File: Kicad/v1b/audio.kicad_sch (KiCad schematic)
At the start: 39 parts, among them U16 74HC139, U17 74HC153, U18 74HC670, U19 74HC670, U20 82C54, U21 82C54 (PLCC), U22 74HC165, U23 74HC165, U24 74HC165, U25 74HC165

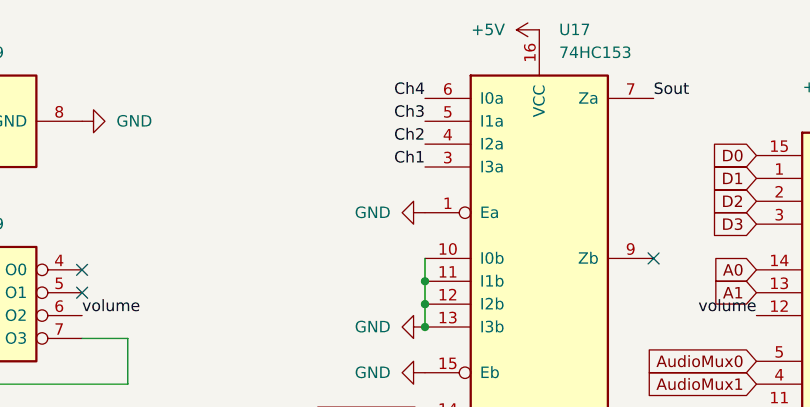
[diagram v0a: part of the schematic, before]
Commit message: Video ROM update, cart files, v1b main board
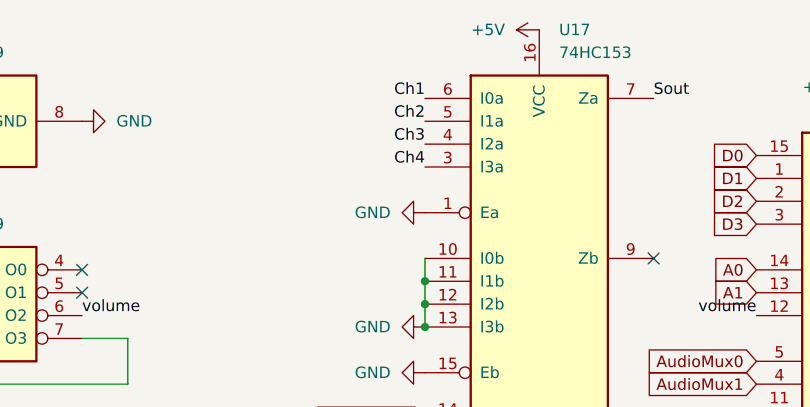
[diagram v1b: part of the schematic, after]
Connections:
- net Ch1: now also U17.6 (I0a); no longer U17.3 (I3a)
- net Ch2: now also U17.5 (I1a); no longer U17.4 (I2a)
- net Ch3: now also U17.4 (I2a); no longer U17.5 (I1a)
- net Ch4: now also U17.3 (I3a); no longer U17.6 (I0a)
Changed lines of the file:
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@@
     (effects (font (size 1.27 1.27)) (justify right bottom))
   )
-  (label "Ch1" (at 99.06 34.29 180) (fields_autoplaced)
+  (label "Ch1" (at 99.06 26.67 180) (fields_autoplaced)
     (effects (font (size 1.27 1.27)) (justify right bottom))
   )
@@
     (effects (font (size 1.27 1.27)) (justify left bottom))
   )
-  (label "Ch2" (at 99.06 31.75 180) (fields_autoplaced)
+  (label "Ch2" (at 99.06 29.21 180) (fields_autoplaced)
     (effects (font (size 1.27 1.27)) (justify right bottom))
   )
@@
     (effects (font (size 1.27 1.27)) (justify left bottom))
   )
-  (label "Ch4" (at 99.06 26.67 180) (fields_autoplaced)
+  (label "Ch4" (at 99.06 34.29 180) (fields_autoplaced)
     (effects (font (size 1.27 1.27)) (justify right bottom))
   )
@@
     (effects (font (size 1.27 1.27)) (justify left bottom))
   )
-  (label "Ch3" (at 99.06 29.21 180) (fields_autoplaced)
+  (label "Ch3" (at 99.06 31.75 180) (fields_autoplaced)
     (effects (font (size 1.27 1.27)) (justify right bottom))
   )
